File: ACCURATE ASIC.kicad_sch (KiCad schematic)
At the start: 51 parts, among them IC1 CERN_aCCURATE2_A_Chip1, IC2 AD817ARZ, IC3 DAC7578SRGE, IC4 AD817ARZ, IC5 AD817ARZ, J12 Conn_02x03_Counter_Clockwise, J14 Conn_01x03

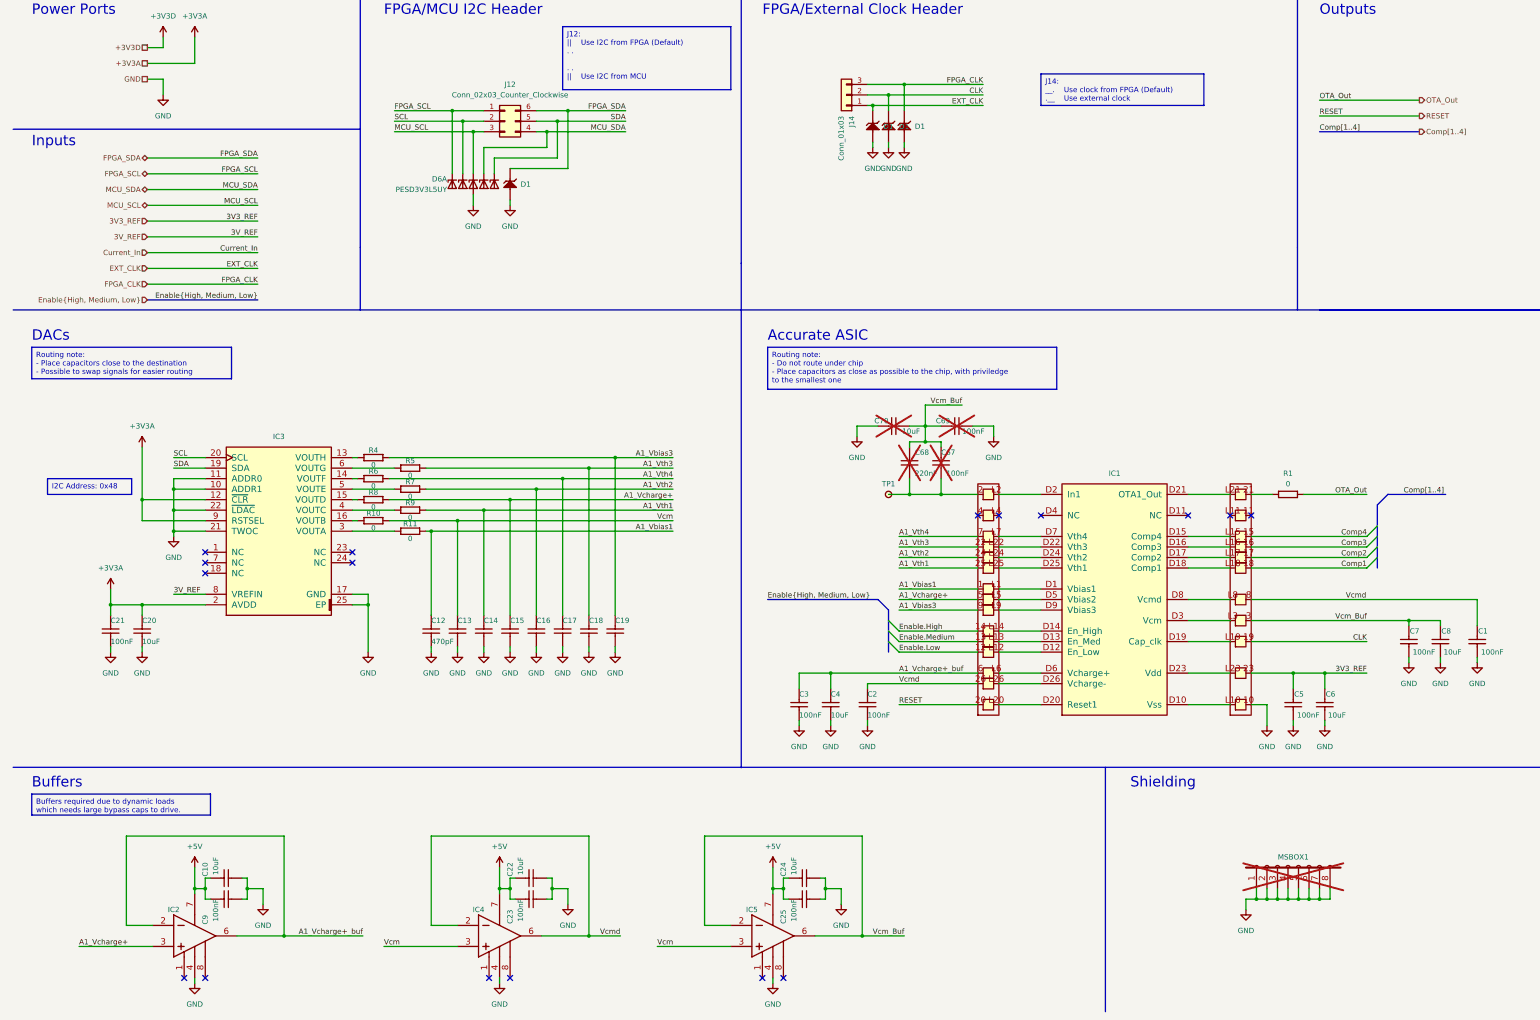
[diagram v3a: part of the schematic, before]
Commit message: Added triax connector, added test points, fixed some mistakes
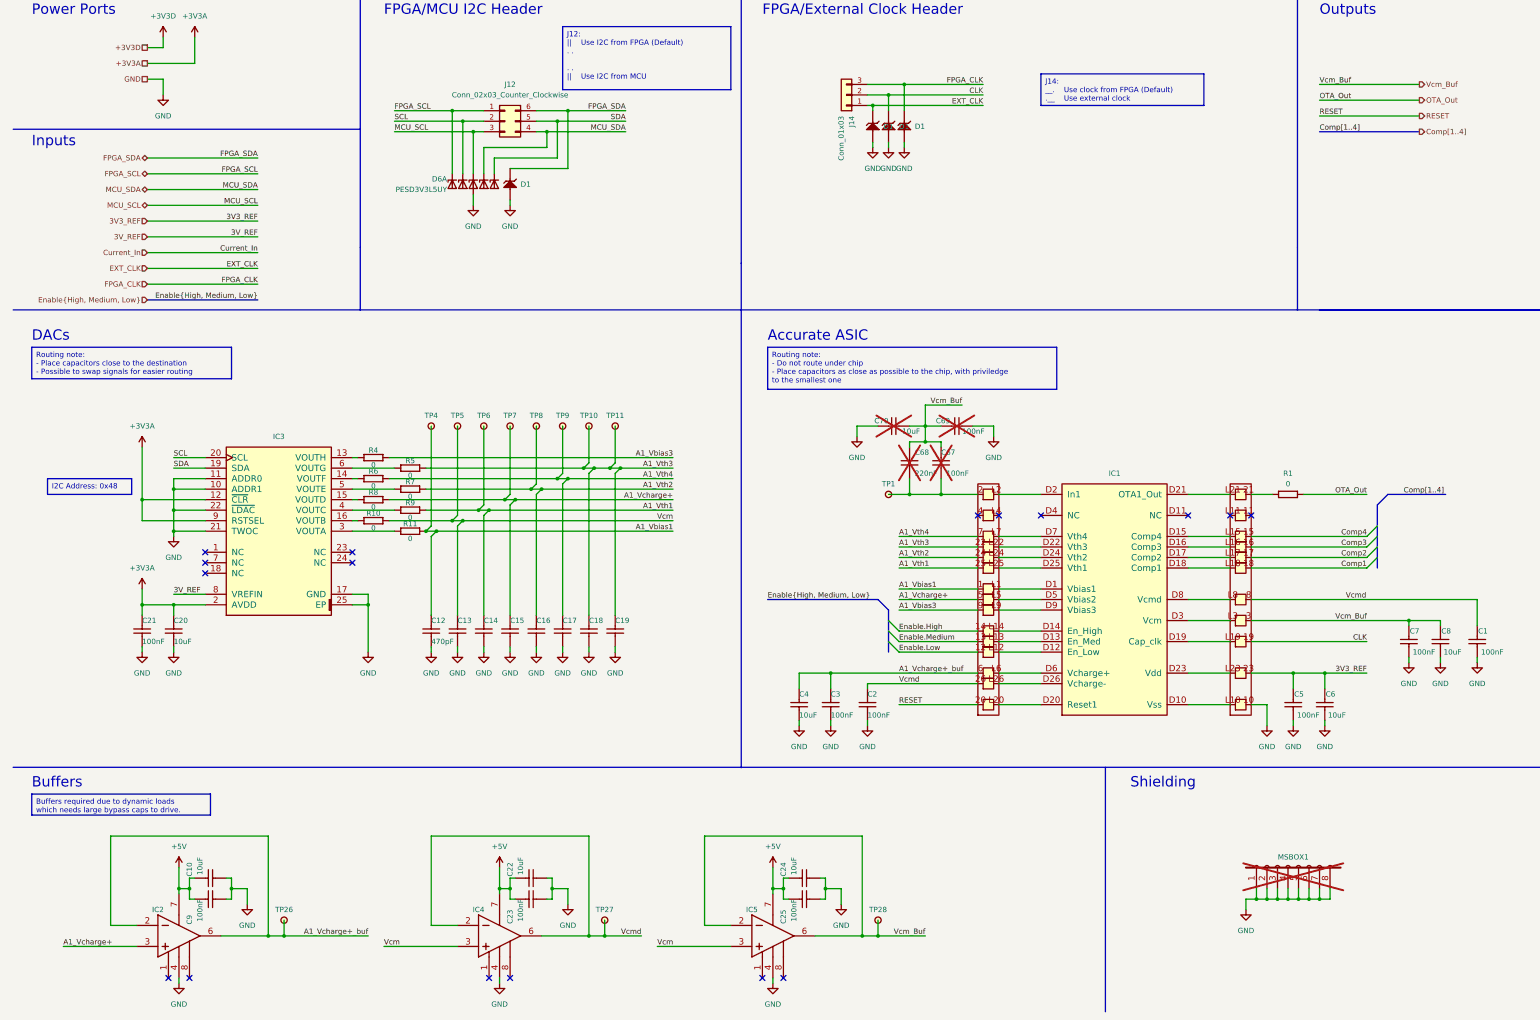
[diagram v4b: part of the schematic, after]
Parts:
- added TP10, TP11, TP26, TP27, TP28, TP4, TP5, TP6, TP7, TP8, TP9: SMD_PAD_1.27X1.27MM, Pads:TPS127, symbol Pads:SMD_PAD_1.27X1.27MM
- J12: footprint (none) -> Connector_PinHeader_2.54mm:PinHeader_2x05_P2.54mm_Vertical
- J14: footprint (none) -> Connector_PinHeader_2.54mm:PinHeader_1x03_P2.54mm_Vertical
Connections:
- net A1_Vbias1: now also TP4.1
- net A1_Vbias3: no longer C19.1
- net A1_Vcharge+: now also TP7.1
- net A1_Vcharge+_buf: now also TP26.1
- net A1_Vth1: now also TP6.1
- net A1_Vth2: now also TP8.1
- net A1_Vth3: now also C19.1, TP10.1, TP11.1
- net A1_Vth4: now also TP9.1
- net Vcm: now also TP5.1
- net Vcm_Buf: now also TP28.1
- net Vcmd: now also TP27.1
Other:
- moved on the sheet: C10, C20, C21, C3, C4, C9, IC2

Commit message: Polished the schematic a bit
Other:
- moved on the sheet: C12, C13, C14, C15, C16, C17, C18, C19, D1, J14, TP10, TP11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

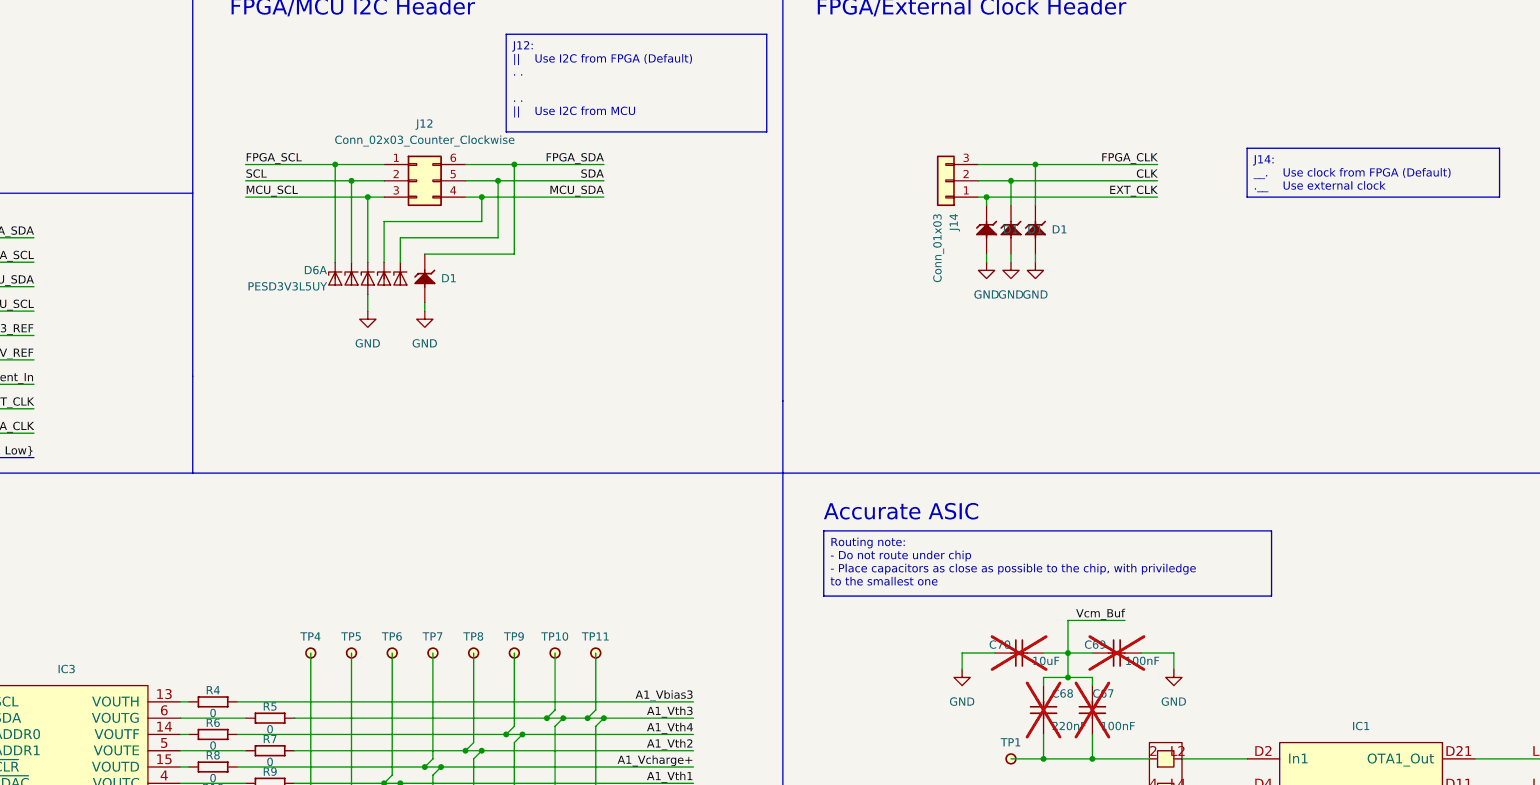
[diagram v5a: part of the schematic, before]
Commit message: Added FPGA prog connector, FPGA UART to USB2Serial IC, RGB LED, fixed mismatch between header symbol and footprint, added more notes, added jumpers
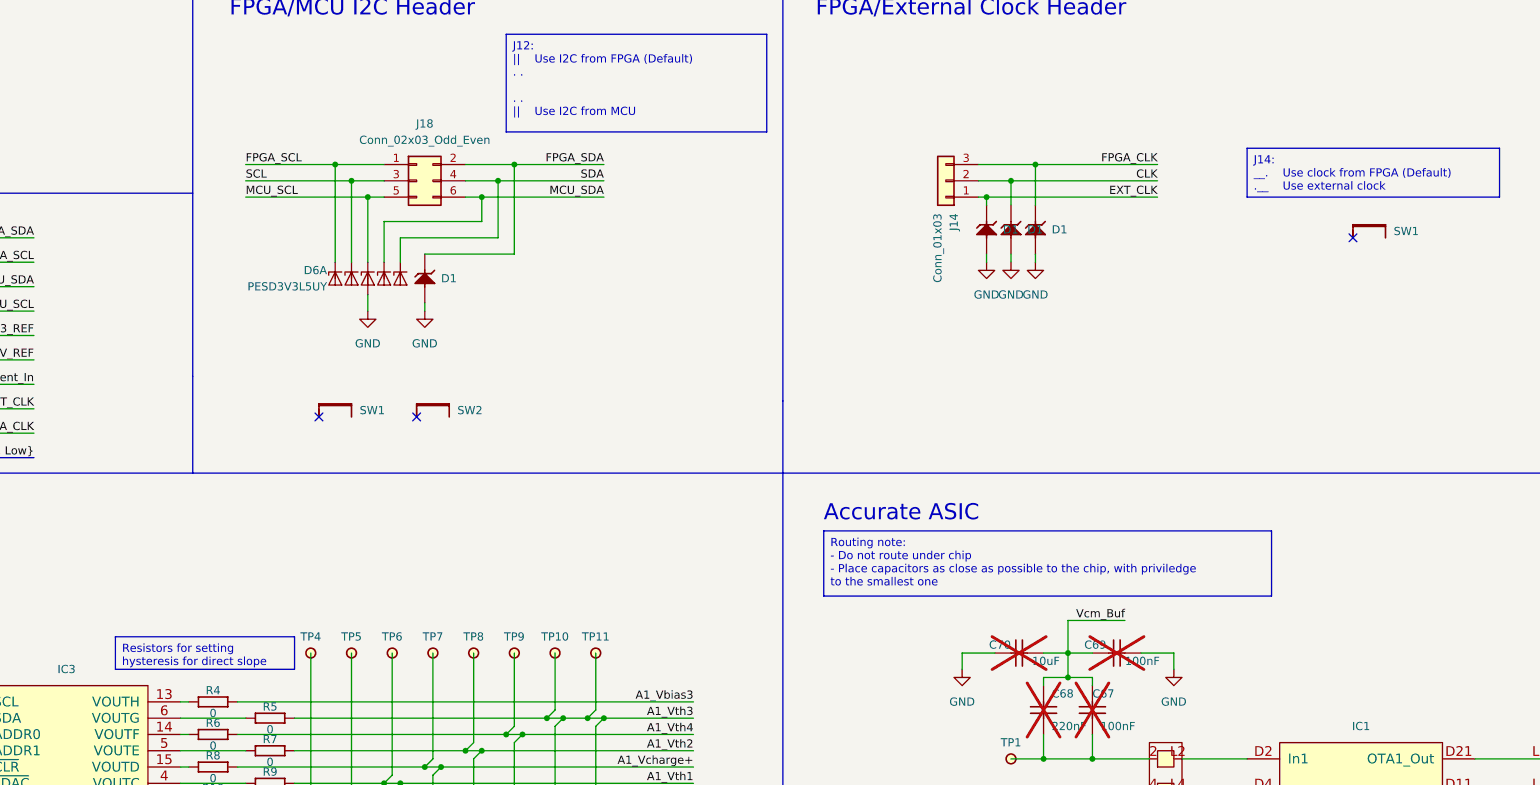
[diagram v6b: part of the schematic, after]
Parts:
- removed J12: Conn_02x03_Counter_Clockwise, Connector_PinHeader_2.54mm:PinHeader_2x05_P2.54mm_Vertical, symbol Connector_Generic:Conn_02x03_Counter_Clockwise
- added J18: Conn_02x03_Odd_Even, Connector_PinHeader_2.54mm:PinHeader_2x03_P2.54mm_Vertical, symbol Connector_Generic:Conn_02x03_Odd_Even
- added SW1 (x2), SW2: HARWIN_M50-1900005, symbol HARWIN:HARWIN_M50-1900005
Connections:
- net FPGA_SCL: now also J18.1 (Pin_1)
- net FPGA_SDA: now also J18.2 (Pin_2)
- net MCU_SCL: now also J18.5 (Pin_5)
- net MCU_SDA: now also J18.6 (Pin_6)
- net SCL: now also J18.3 (Pin_3)
- net SDA: now also J18.4 (Pin_4)
- no-connect marks 17 -> 20

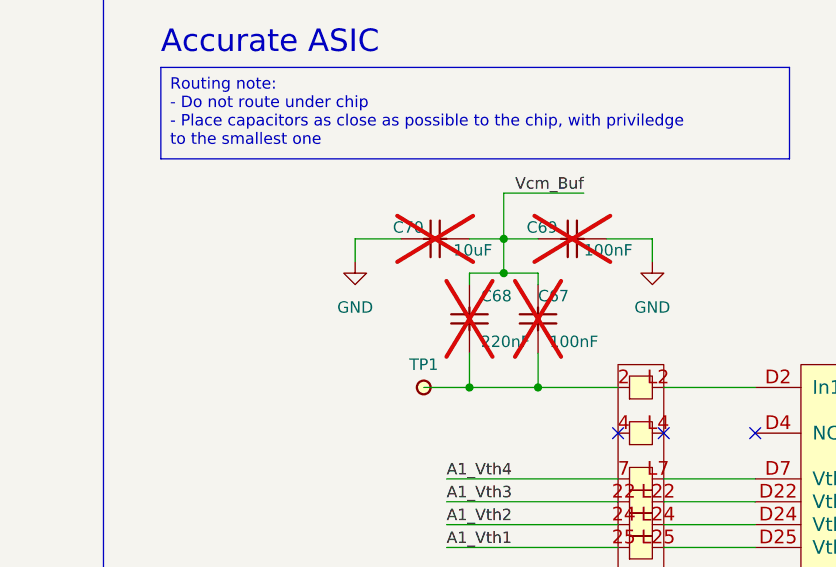
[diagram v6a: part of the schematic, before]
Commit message: Added current input to Accurate, specified shielding around current input in note
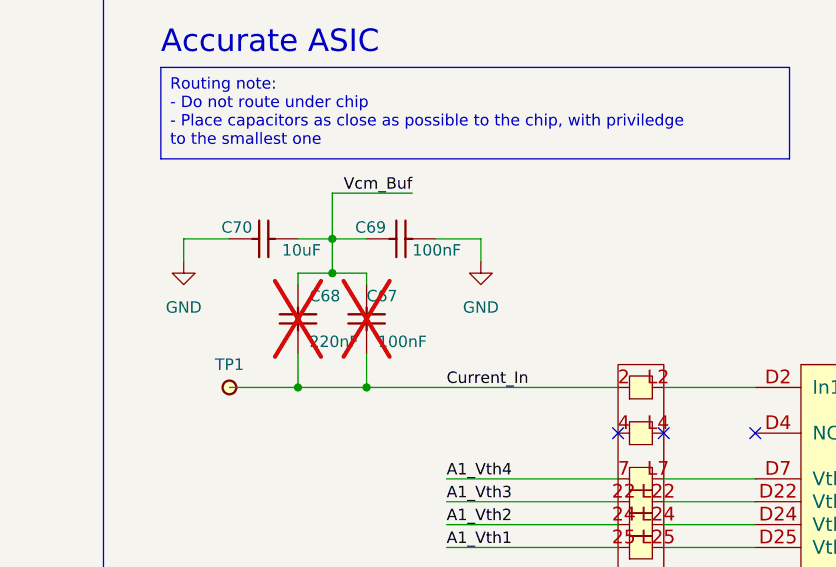
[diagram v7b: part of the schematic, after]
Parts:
- C69, C70: now fitted
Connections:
- net Current_In: now also C67.2, C68.2, IC1.2, TP1.1
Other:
- moved on the sheet: C67, C68, TP1

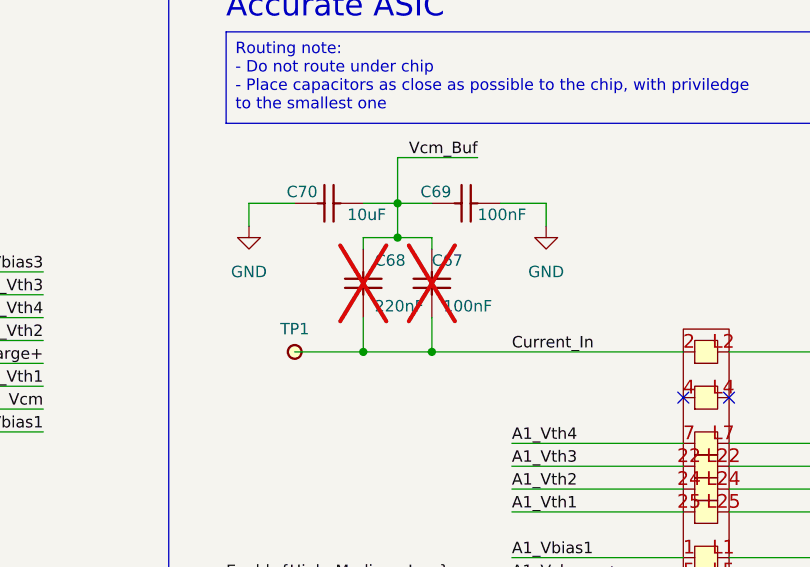
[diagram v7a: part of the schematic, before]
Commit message: Added more routing notes for input connector
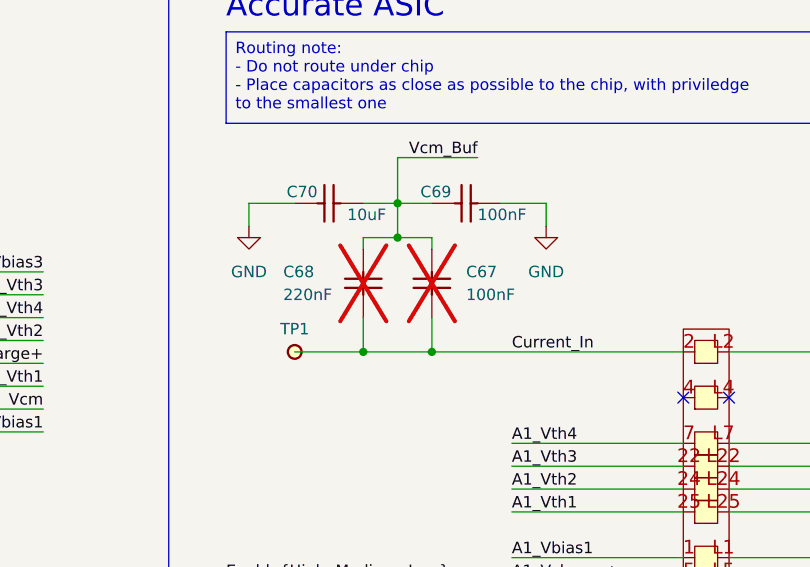
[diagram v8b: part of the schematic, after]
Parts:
- removed C67: CC0603_100NF_50V_10%_X7R, Capacitors SMD:CAPC1608X87N, symbol Capacitors SMD:CC0603_100NF_50V_10%_X7R
- removed C68: CC0603_220NF_10V_10%_X7R, Capacitors SMD:CAPC1608X87N, symbol Capacitors SMD:CC0603_220NF_10V_10%_X7R
- added C67: CC1206_100NF_50V_10%_X7R, Capacitors SMD:CAPC3216X140N, symbol Capacitors SMD:CC1206_100NF_50V_10%_X7R
- added C68: CC1206_220NF_16V_10%_X7R, Capacitors SMD:CAPC3216X140N, symbol Capacitors SMD:CC1206_220NF_16V_10%_X7R
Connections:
- net Current_In: now also C67.2, C68.2
- net Vcm_Buf: now also C67.1, C68.1
